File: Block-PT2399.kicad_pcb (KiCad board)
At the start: 2 copper layers, 65 x 65 mm, 28 parts, among them J1 Sig_in, J2 Sig_out, J3 Sig_gnd, J4 +9V, Q1 2N3819, U1 LM7805_TO220, U2 PT2399

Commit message: implement pin-2 hack and anti-latch
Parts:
- added C10: 100nF, Capacitor_THT:C_Disc_D3.0mm_W1.6mm_P2.50mm, F.Cu at (125.0, 124.0)
- added C11: 10uF, Capacitor_THT:CP_Radial_D5.0mm_P2.00mm, F.Cu at (131.5, 135.5)
- added C12: 10uF, Capacitor_THT:CP_Radial_D4.0mm_P2.00mm, F.Cu at (144.5, 130.0)
- added D1: 1N4001, Diode_THT:D_DO-41_SOD81_P10.16mm_Horizontal, F.Cu at (124.5, 136.9)
- added D2: 1N4148, Diode_THT:D_DO-35_SOD27_P7.62mm_Horizontal, F.Cu at (154.0, 137.3)
- added Q2: BC337, Package_TO_SOT_THT:TO-92_Inline, F.Cu at (150.6, 123.2)
- R4: value 4.7k -> 100k; footprint Resistor_THT:R_Axial_DIN0207_L6.3mm_D2.5mm_P10.16mm_Horizontal -> Resistor_THT:R_Axial_DIN0204_L3.6mm_D1.6mm_P5.08mm_Horizontal
- RV1: value B50k -> B100k
- moved RV1 18.3 mm to (138.0, 120.9), turned to 90 degrees
- moved R4 10.9 mm to (148.0, 132.4), turned to -90 degrees
- moved C4 5.70 mm to (149.0, 112.5), turned to 0 degrees
- moved J2 4.92 mm to (160.0, 104.0)
- moved C3 4.61 mm to (149.0, 117.0), turned to 0 degrees
- moved J4 4.53 mm to (134.5, 144.5)
- moved J3 4.50 mm to (117.0, 144.5)
- moved C7 3.91 mm to (153.5, 95.5)
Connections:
- C2 pad 1: Net-(U1-VO) -> +5V
- R4 pad 1: Net-(R4-Pad1) -> Net-(D2-A)
- R4 pad 2: Net-(U2-VCO) -> +5V
- RV1 pad 1: Net-(U2-DGND) -> Net-(U2-REF)
- RV1 pad 2: Net-(R4-Pad1) -> Net-(U2-REF)
- RV1 pad 3: Net-(R4-Pad1) -> GND
- U1 pad 1: +9V -> Net-(D1-K)
- U1 pad 3: Net-(U1-VO) -> +5V
- U2 pad 1: Net-(U1-VO) -> +5V
- U2 pad 2: unconnected-(U2-REF-Pad2) -> Net-(U2-REF)
- U2 pad 4: Net-(U2-DGND) -> GND
- U2 pad 6: Net-(U2-VCO) -> Net-(Q2-C)
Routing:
- net GND: track 139.9 -> 211.0 mm
- net +5V: track 0.00 -> 50.5 mm
- net Net-(U2-DGND): track 27.3 -> 0.00 mm
- net Net-(D2-A): track 0.00 -> 18.8 mm
- net Net-(R4-Pad1): track 16.6 -> 0.00 mm
- net Net-(Q2-C): track 0.00 -> 16.4 mm
- net Net-(U1-VO): track 15.9 -> 0.00 mm
- net Net-(D1-K): track 0.00 -> 14.6 mm
- net Net-(U2-REF): track 0.00 -> 12.7 mm
- net +9V: track 78.8 -> 70.6 mm
- net Net-(U2-VCO): track 4.51 -> 0.00 mm
- net Net-(U2-CC1): track 4.06 -> 6.88 mm
- net Net-(U2-CC0): track 6.25 -> 4.13 mm
- net Net-(U2-LPF1-OUT): track 40.1 -> 41.2 mm

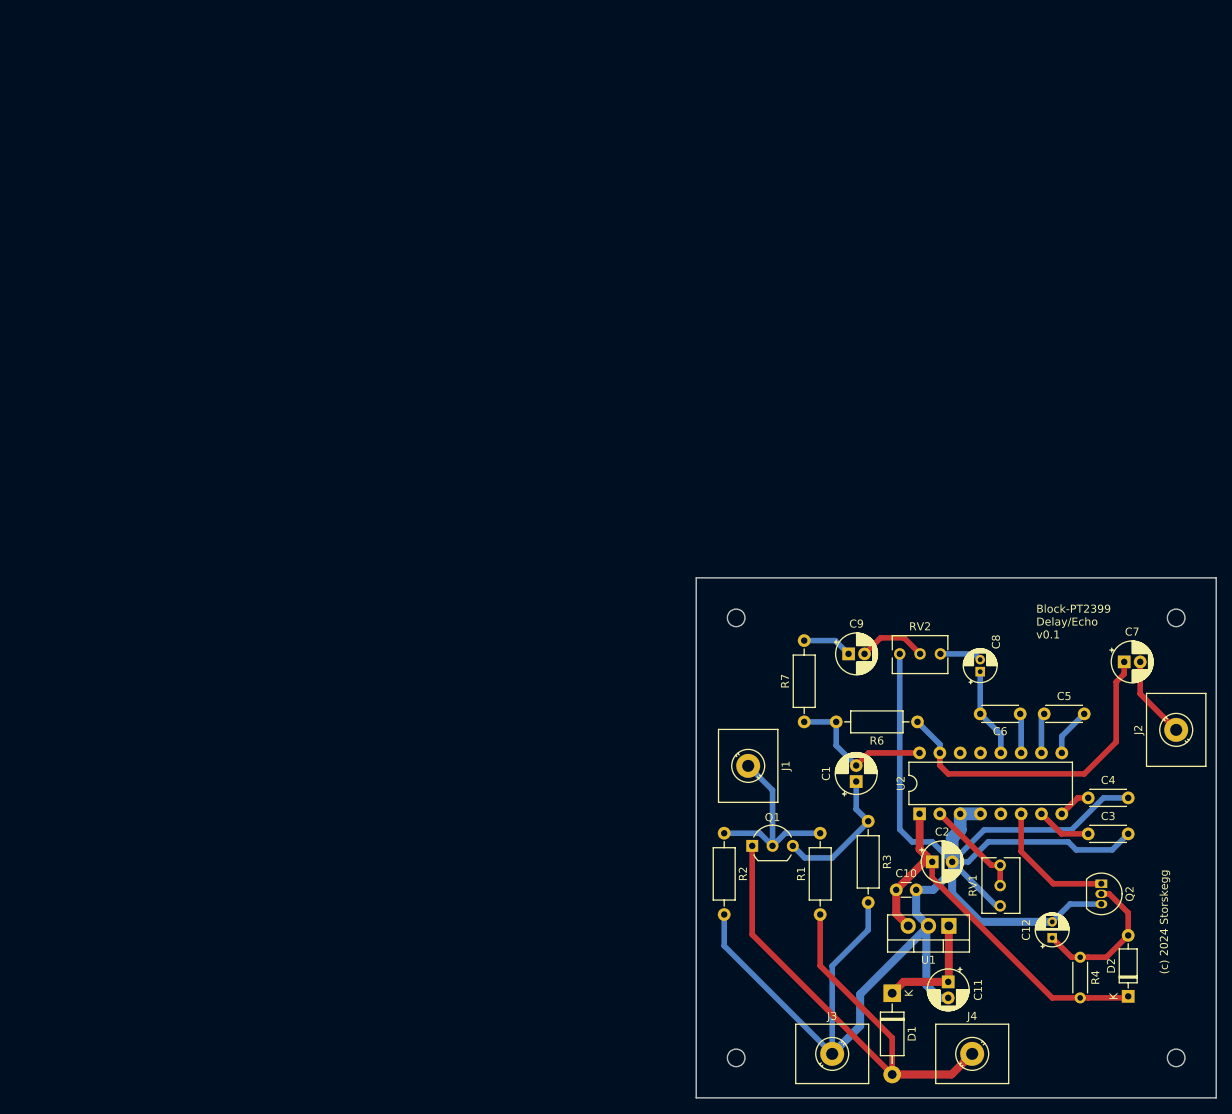
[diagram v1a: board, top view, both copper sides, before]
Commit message: working on redoing board size and layout, dropped the diode
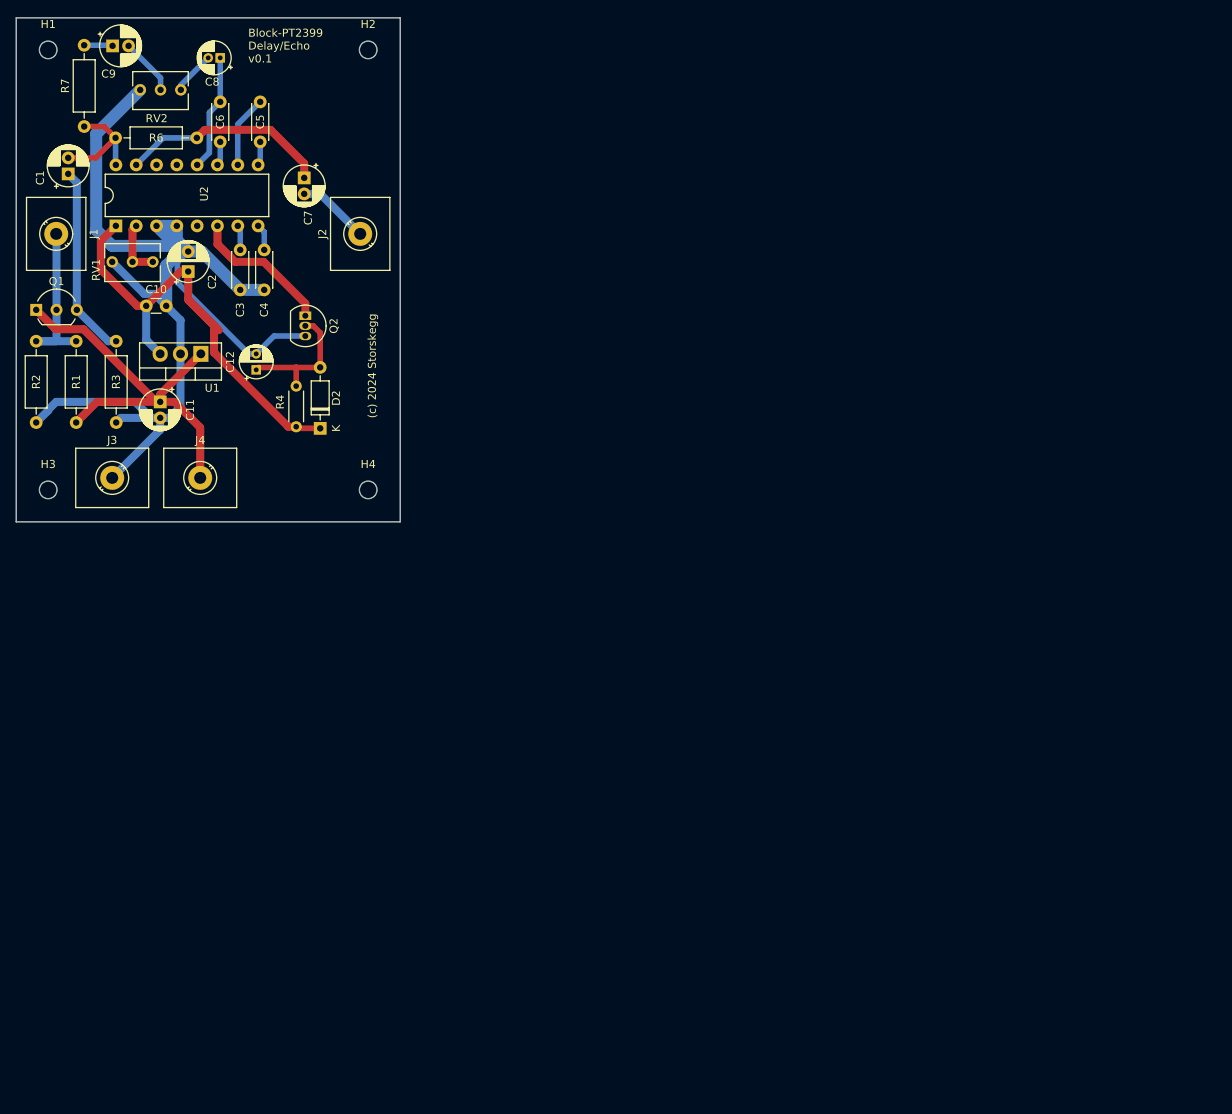
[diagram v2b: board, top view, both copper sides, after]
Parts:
- removed D1: 1N4001, Diode_THT:D_DO-41_SOD81_P10.16mm_Horizontal
- removed REF** (x4): MountingHole_2.2mm_M2, MountingHole:MountingHole_2.2mm_M2
- added H1: MountingHole, MountingHole:MountingHole_2.2mm_M2, F.Cu at (19.0, 19.0)
- added H2: MountingHole, MountingHole:MountingHole_2.2mm_M2, F.Cu at (59.0, 19.0)
- added H3: MountingHole, MountingHole:MountingHole_2.2mm_M2, F.Cu at (19.0, 74.0)
- added H4: MountingHole, MountingHole:MountingHole_2.2mm_M2, F.Cu at (59.0, 74.0)
- moved RV1 130.0 mm to (32.1, 45.5), turned to 0 degrees
- moved C3 128.7 mm to (43.0, 44.0), turned to -90 degrees
- moved U2 124.5 mm to (27.5, 41.0)
- moved C1 124.4 mm to (21.5, 34.5)
- moved C5 124.3 mm to (45.5, 25.5), turned to -90 degrees
- moved C4 123.7 mm to (46.0, 44.0), turned to -90 degrees
- moved D2 123.5 mm to (53.0, 66.3)
- moved C6 122.9 mm to (40.5, 30.5), turned to 90 degrees
- moved C11 122.3 mm to (33.0, 63.0)
- moved C12 122.2 mm to (45.0, 59.0)
- moved Q2 122.2 mm to (51.1, 52.2)
- moved C8 122.1 mm to (40.5, 20.0), turned to 180 degrees
- moved R4 121.2 mm to (50.0, 61.0)
- moved J4 120.4 mm to (38.0, 72.5)
- moved J2 119.4 mm to (58.0, 42.0)
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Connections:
- C11 pad 1: Net-(D1-K) -> +9V
- U1 pad 1: Net-(D1-K) -> +9V
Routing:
- net GND: track 211.0 -> 147.7 mm
- net +9V: track 70.6 -> 52.6 mm
- net Net-(D1-K): track 14.6 -> 0.00 mm
- net Net-(U2-LPF1-OUT): track 41.2 -> 27.6 mm
- net +5V: track 50.5 -> 61.3 mm
- net Net-(Q1-S): track 17.6 -> 24.0 mm
- net Net-(U2-REF): track 12.7 -> 7.23 mm
- net Net-(U2-LPF1-IN): track 19.1 -> 14.8 mm
- net Net-(U2-CC1): track 6.88 -> 2.70 mm
- net Net-(U2-OP1-IN): track 5.02 -> 9.04 mm
- net Net-(U2-OP1-OUT): track 6.04 -> 2.62 mm
- net Net-(U2-OP2-OUT): track 11.2 -> 14.6 mm
- net Net-(C9-Pad1): track 6.23 -> 3.46 mm
- net Net-(U2-OP2-IN): track 4.93 -> 3.02 mm
- net Net-(D2-A): track 18.8 -> 17.0 mm
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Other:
- board size 65 x 65 mm -> 48 x 63 mm

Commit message: widen traces to lower trace impedances
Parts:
- moved Q2 7.99 mm to (43.2, 53.4), turned to 0 degrees
- moved C12 1.80 mm to (44.0, 60.5)
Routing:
- net GND: track 147.7 -> 162.5 mm
- net Net-(Q2-C): track 17.9 -> 13.6 mm
- net +5V: track 61.3 -> 58.7 mm
- net Net-(U2-OP2-OUT): track 14.6 -> 16.5 mm
- net Net-(D2-A): track 17.0 -> 18.2 mm
- net +9V: track 52.6 -> 53.4 mm
- net Net-(U2-LPF1-OUT): track 27.6 -> 26.8 mm
